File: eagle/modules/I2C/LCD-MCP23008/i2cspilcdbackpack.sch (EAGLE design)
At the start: 17 parts, among them IC1 MCP2300X/P, J2 RJ12RIGHTANGLE-I2C, J3 RJ12RIGHTANGLE-I2C

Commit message: Update
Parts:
- added X1: HD44780LCD-1602, adafruit:HD44780LCD-1602
- C2: device adafruit:C-USC0805K -> adafruit:C-USC1206
- R1, R2, R3, R4, R5, R7: device adafruit:R-US_R0805 -> adafruit:R-US_M1206
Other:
- moved on the sheet: A0, A1, A2, C1, C2, IC1, J2, J3, JP1, Q1, R1, R2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

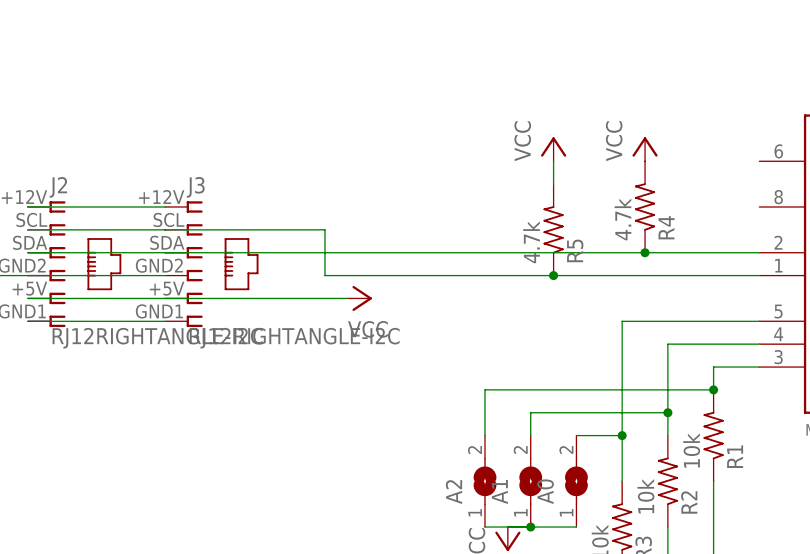
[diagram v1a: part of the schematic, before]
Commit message: Remove via close to rj12
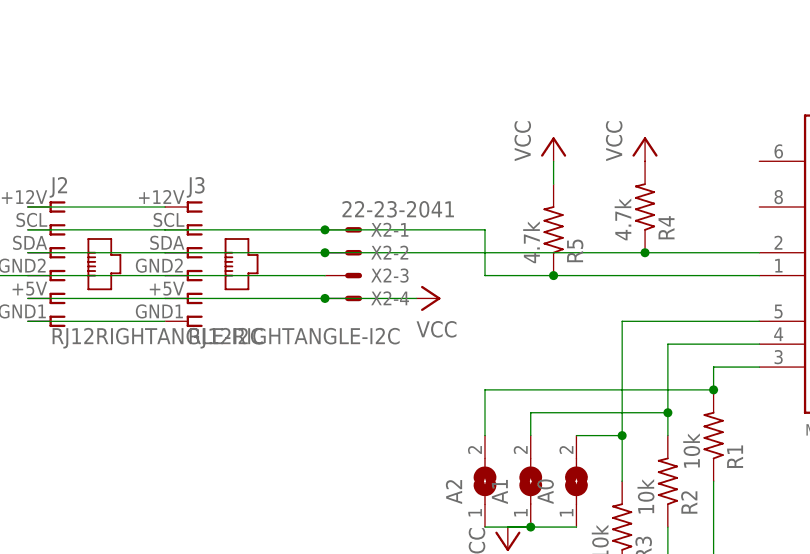
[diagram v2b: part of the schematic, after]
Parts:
- added X2: 22-23-2041, con-molex:22-23-2041
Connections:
- net CLOCK: now also X2-1.S
- net DATA: now also X2-2.S
- net GND: now also X2-3.S
- net VCC: now also X2-4.S
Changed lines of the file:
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@@
 <part name="R6" library="pot" deviceset="TRIM_EU-" device="CA9V"/>
 <part name="X1" library="adafruit" deviceset="HD44780LCD" device="-1602"/>
+<part name="X2" library="con-molex" deviceset="22-23-2041" device=""/>
 </parts>
 <sheets>
@@
 <instance part="P+7" gate="VCC" x="38.1" y="91.44"/>
 <instance part="GND6" gate="1" x="-30.48" y="73.66" rot="MR0"/>
-<instance part="P+9" gate="VCC" x="17.78" y="73.66" rot="MR90"/>
+<instance part="P+9" gate="VCC" x="25.4" y="73.66" rot="MR90"/>
 <instance part="Q1" gate="G$1" x="157.48" y="38.1" smashed="yes" rot="MR0">
 <attribute name="NAME" x="152.4" y="38.1" size="1.778" layer="95" rot="MR90"/>
@@
 <instance part="R6" gate="1" x="96.52" y="55.88" rot="R270"/>
 <instance part="X1" gate="G$1" x="127" y="2.54"/>
+<instance part="X2" gate="-1" x="15.24" y="81.28"/>
+<instance part="X2" gate="-2" x="15.24" y="78.74"/>
+<instance part="X2" gate="-3" x="15.24" y="76.2"/>
+<instance part="X2" gate="-4" x="15.24" y="73.66"/>
 </instances>
 <busses>
@@
 <pinref part="J2" gate="G$1" pin="5"/>
 <wire x1="-5.08" y1="73.66" x2="-20.32" y2="73.66" width="0.1524" layer="91"/>
-<wire x1="-5.08" y1="73.66" x2="15.24" y2="73.66" width="0.1524" layer="91"/>
+<wire x1="-5.08" y1="73.66" x2="12.7" y2="73.66" width="0.1524" layer="91"/>
+<pinref part="X2" gate="-4" pin="S"/>
+<wire x1="12.7" y1="73.66" x2="22.86" y2="73.66" width="0.1524" layer="91"/>
+<junction x="12.7" y="73.66"/>
 </segment>
 <segment>
@@
 <pinref part="GND6" gate="1" pin="GND"/>
 <wire x1="-30.48" y1="76.2" x2="-20.32" y2="76.2" width="0.1524" layer="91"/>
+<pinref part="X2" gate="-3" pin="S"/>
+<wire x1="-5.08" y1="76.2" x2="12.7" y2="76.2" width="0.1524" layer="91"/>
 </segment>
 <segment>
@@
 <segment>
 <wire x1="60.96" y1="76.2" x2="38.1" y2="76.2" width="0.1524" layer="91"/>
-<wire x1="38.1" y1="76.2" x2="12.7" y2="76.2" width="0.1524" layer="91"/>
+<wire x1="38.1" y1="76.2" x2="30.48" y2="76.2" width="0.1524" layer="91"/>
 <junction x="38.1" y="76.2"/>
 <pinref part="IC1" gate="G$1" pin="SCL"/>
 <pinref part="R5" gate="G$1" pin="1"/>
-<wire x1="12.7" y1="76.2" x2="12.7" y2="81.28" width="0.1524" layer="91"/>
+<wire x1="30.48" y1="76.2" x2="30.48" y2="81.28" width="0.1524" layer="91"/>
 <pinref part="J2" gate="G$1" pin="2"/>
 <pinref part="J3" gate="G$1" pin="2"/>
 <wire x1="-20.32" y1="81.28" x2="-5.08" y2="81.28" width="0.1524" layer="91"/>
+<wire x1="30.48" y1="81.28" x2="12.7" y2="81.28" width="0.1524" layer="91"/>
+<pinref part="X2" gate="-1" pin="S"/>
 <wire x1="12.7" y1="81.28" x2="-5.08" y2="81.28" width="0.1524" layer="91"/>
+<junction x="12.7" y="81.28"/>
 </segment>
 </net>
 <net name="DATA" class="0">
 <segment>
-<wire x1="-5.08" y1="78.74" x2="48.26" y2="78.74" width="0.1524" layer="91"/>
+<wire x1="-5.08" y1="78.74" x2="12.7" y2="78.74" width="0.1524" layer="91"/>
+<wire x1="12.7" y1="78.74" x2="48.26" y2="78.74" width="0.1524" layer="91"/>
 <wire x1="48.26" y1="78.74" x2="60.96" y2="78.74" width="0.1524" layer="91"/>
 <junction x="48.26" y="78.74"/>
@@
 <pinref part="J2" gate="G$1" pin="3"/>
 <wire x1="-5.08" y1="78.74" x2="-20.32" y2="78.74" width="0.1524" layer="91"/>
-</segment>
-</net>
+<pinref part="X2" gate="-2" pin="S"/>
+<junction x="12.7" y="78.74"/>
+</segment>
+</net>
